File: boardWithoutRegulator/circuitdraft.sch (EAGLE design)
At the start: 50 parts, among them IC1 BQ25887RGER, IC2 TPS54627DDAR, Q1 16 MHz

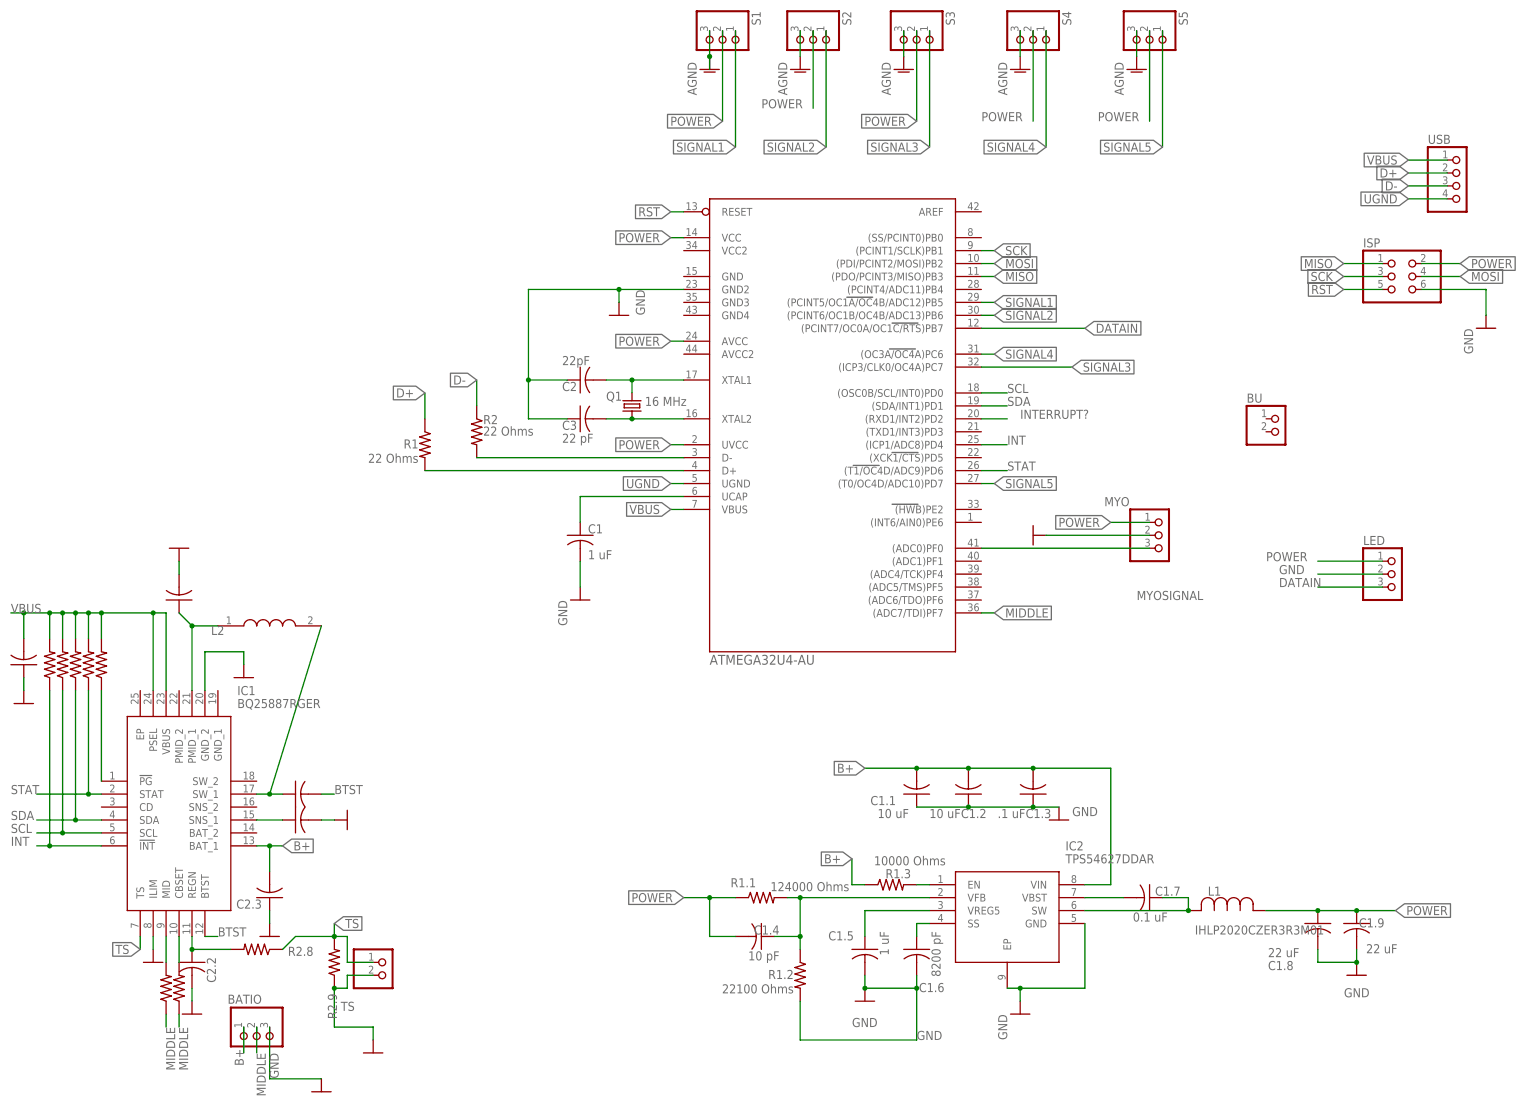
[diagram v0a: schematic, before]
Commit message: Started to route and made power more centralized
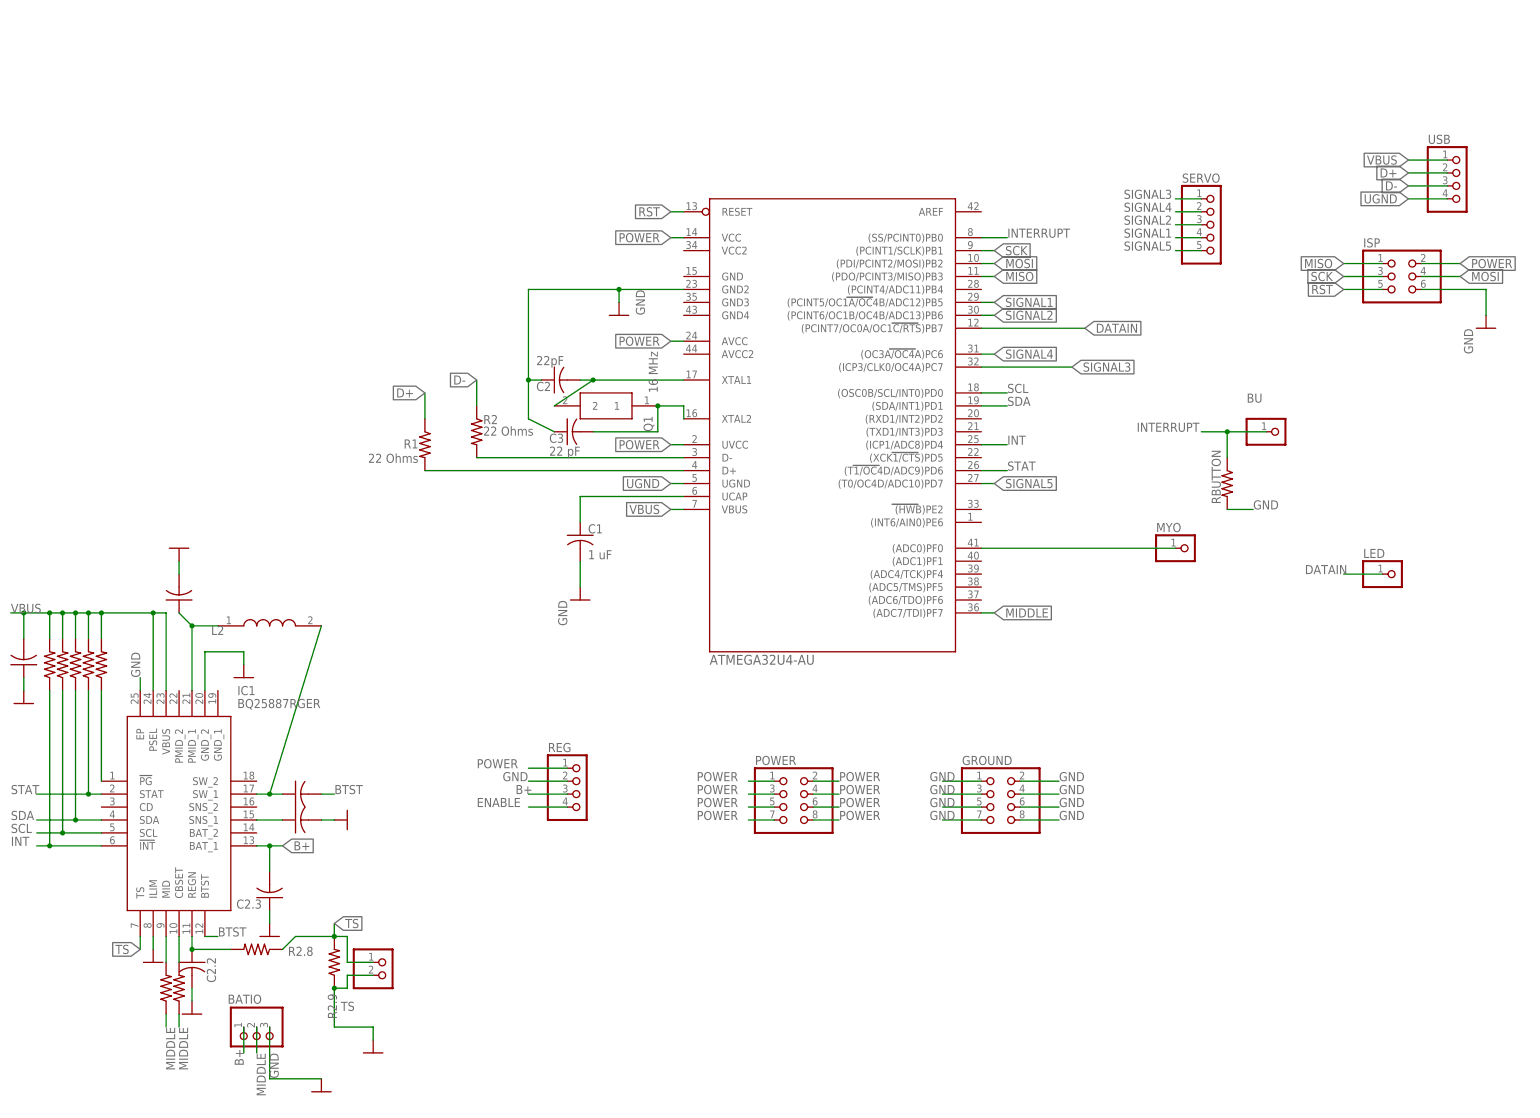
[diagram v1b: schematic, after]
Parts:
- removed C1.1, C1.2: 10 uF, rcl:C-USC0805
- removed C1.3: .1 uF, rcl:C-USC0805
- removed C1.4: 10 pF, rcl:C-USC0805
- removed C1.5: 1 uF, rcl:C-USC0603
- removed C1.6: 8200 pF, rcl:C-USC0603
- removed C1.7: 0.1 uF, rcl:C-USC0805
- removed C1.8, C1.9: 22 uF, rcl:C-USC0805
- removed IC2: TPS54627DDAR, TPS54627DDAR:TPS54627DDAR
- removed L1: IHLP2020CZER3R3M01, ind2:IHLP2020CZER3R3M01
- removed R1.1: 124000 Ohms, rcl:R-US_R0603
- removed R1.2: 22100 Ohms, rcl:R-US_R0603
- removed R1.3: 10000 Ohms, rcl:R-US_R0603
- removed S1, S2, S3, S4, S5: (no value), pinhead:PINHD-1X3
- added GROUND, POWER: (no value), pinhead:PINHD-2X4
- added RBUTTON: 220 Ohm, rcl:R-US_R0603
- added REG: (no value), pinhead:PINHD-1X4
- added SERVO: (no value), pinhead:PINHD-1X5
- BU: device pinhead:PINHD-1X2 -> pinhead:PINHD-1X1
- C1, C2, C2.1, C2.2, C2.3, C2.4, C2.5, C2.6, C3: device rcl:C-USC0805 -> rcl:C-USC0603
- LED, MYO: device pinhead:PINHD-1X3 -> pinhead:PINHD-1X1
- Q1: device crystal-geyer_V1_0:KX-5 -> SamacSys_Parts:ECS-160-18-23G-JGN-TR
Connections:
- removed net INTERRUPT?: U$1.(RXD1/INT2)PD2
- removed net N$1: IC2.EN, R1.3.2
- removed net N$11: C1.4.1, IC2.VFB, R1.1.2, R1.2.1
- removed net N$13: C1.5.1, IC2.VREG5
- removed net N$14: C1.7.1, IC2.SW, L1.2
- removed net N$15: C1.7.2, IC2.VBST
- removed net N$9: C1.6.1, IC2.SS
- new net ENABLE: REG.4
- new net INTERRUPT: BU.1, RBUTTON.1, U$1.(SS/PCINT0)PB0
- net B+: now also REG.3; no longer C1.1.2, C1.2.2, C1.3.2, IC2.VIN, R1.3.1
- net DATAIN: now also LED.1; no longer LED.3
- net GND: now also GROUND.1, GROUND.2, GROUND.3, GROUND.4, GROUND.5, GROUND.6, GROUND.7, GROUND.8, IC1.EP, RBUTTON.2, REG.2; no longer C1.1.1, C1.2.1, C1.3.1, C1.5.2, C1.6.2, C1.8.2, C1.9.2, IC2.EP, IC2.GND, LED.2, MYO.2, R1.2.2, S1.3, S2.3, S3.3, S4.3, S5.3
- net MYOSIGNAL: now also MYO.1; no longer MYO.3
- net POWER: now also POWER.1, POWER.2, POWER.3, POWER.4, POWER.5, POWER.6, POWER.7, POWER.8, REG.1; no longer C1.4.2, C1.8.1, C1.9.1, L1.1, LED.1, MYO.1, R1.1.1, S1.2, S2.2, S3.2, S4.2, S5.2
- net SIGNAL1: now also SERVO.4; no longer S1.1
- net SIGNAL2: now also SERVO.3; no longer S2.1
- net SIGNAL3: now also SERVO.1; no longer S3.1
- net SIGNAL4: now also SERVO.2; no longer S4.1
- net SIGNAL5: now also SERVO.5; no longer S5.1
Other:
- moved on the sheet: C2, C3

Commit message: Fixed it boii
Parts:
- Q1: device SamacSys_Parts:ECS-160-18-23G-JGN-TR -> crystal-geyer_V1_0:KX-5
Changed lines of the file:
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@@
 <part name="AGND2" library="supply1" library_urn="urn:adsk.eagle:library:371" deviceset="GND" device=""/>
 <part name="AGND3" library="supply1" library_urn="urn:adsk.eagle:library:371" deviceset="GND" device=""/>
-<part name="Q1" library="SamacSys_Parts" deviceset="ECS-160-18-23G-JGN-TR" device="" value="16 MHz"/>
+<part name="Q1" library="crystal-geyer_V1_0" library_urn="urn:adsk.eagle:library:203" deviceset="KX" device="-5" package3d_urn="urn:adsk.eagle:package:11926/1" value="16 MHz"/>
 <part name="C2" library="rcl" library_urn="urn:adsk.eagle:library:334" deviceset="C-US" device="C0603" package3d_urn="urn:adsk.eagle:package:23616/2" value="22pF"/>
 <part name="C3" library="rcl" library_urn="urn:adsk.eagle:library:334" deviceset="C-US" device="C0603" package3d_urn="urn:adsk.eagle:package:23616/2" value="22 pF"/>
@@
 <wire x1="137.16" y1="149.86" x2="119.38" y2="149.86" width="0.1524" layer="91"/>
 <pinref part="Q1" gate="G$1" pin="2"/>
-<wire x1="119.38" y1="149.86" x2="111.76" y2="144.78" width="0.1524" layer="91"/>
+<wire x1="119.38" y1="149.86" x2="129.54" y2="144.78" width="0.1524" layer="91"/>
 <pinref part="C2" gate="G$1" pin="2"/>
 <wire x1="119.38" y1="149.86" x2="116.84" y2="149.86" width="0.1524" layer="91"/>
@@
 <pinref part="Q1" gate="G$1" pin="1"/>
 <wire x1="137.16" y1="142.24" x2="137.16" y2="144.78" width="0.1524" layer="91"/>
-<wire x1="137.16" y1="144.78" x2="132.08" y2="144.78" width="0.1524" layer="91"/>
-<wire x1="132.08" y1="144.78" x2="132.08" y2="139.7" width="0.1524" layer="91"/>
-<junction x="132.08" y="144.78"/>
+<wire x1="137.16" y1="144.78" x2="134.62" y2="144.78" width="0.1524" layer="91"/>
+<wire x1="134.62" y1="144.78" x2="132.08" y2="139.7" width="0.1524" layer="91"/>
+<junction x="134.62" y="144.78"/>
 <pinref part="C3" gate="G$1" pin="2"/>
 <wire x1="132.08" y1="139.7" x2="119.38" y2="139.7" width="0.1524" layer="91"/>
